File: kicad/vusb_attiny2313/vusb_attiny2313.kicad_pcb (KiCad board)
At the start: 2 copper layers, 64.9 x 49.4 mm, 24 parts, among them J1 USB_B_Micro, J2 PORT, J3 PORT B, J4 PORT A, Q1 BSS138, SW1 SW_SPST, U1 LM1117-1.8, U2 ATTINY2313-20PU, U3 MCP23S17, Y1 12Mhz

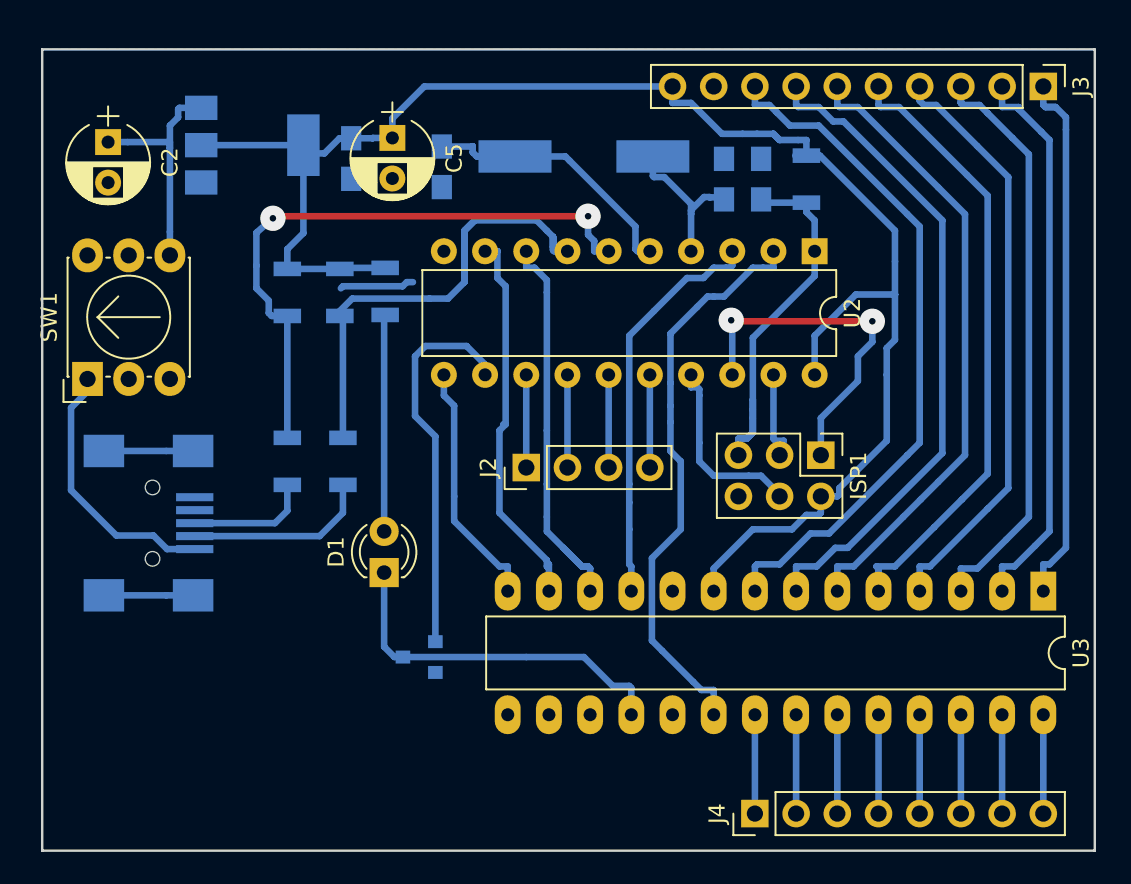
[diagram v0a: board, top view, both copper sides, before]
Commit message: first revision, kernel and avr part work. Kernel code have to be refine
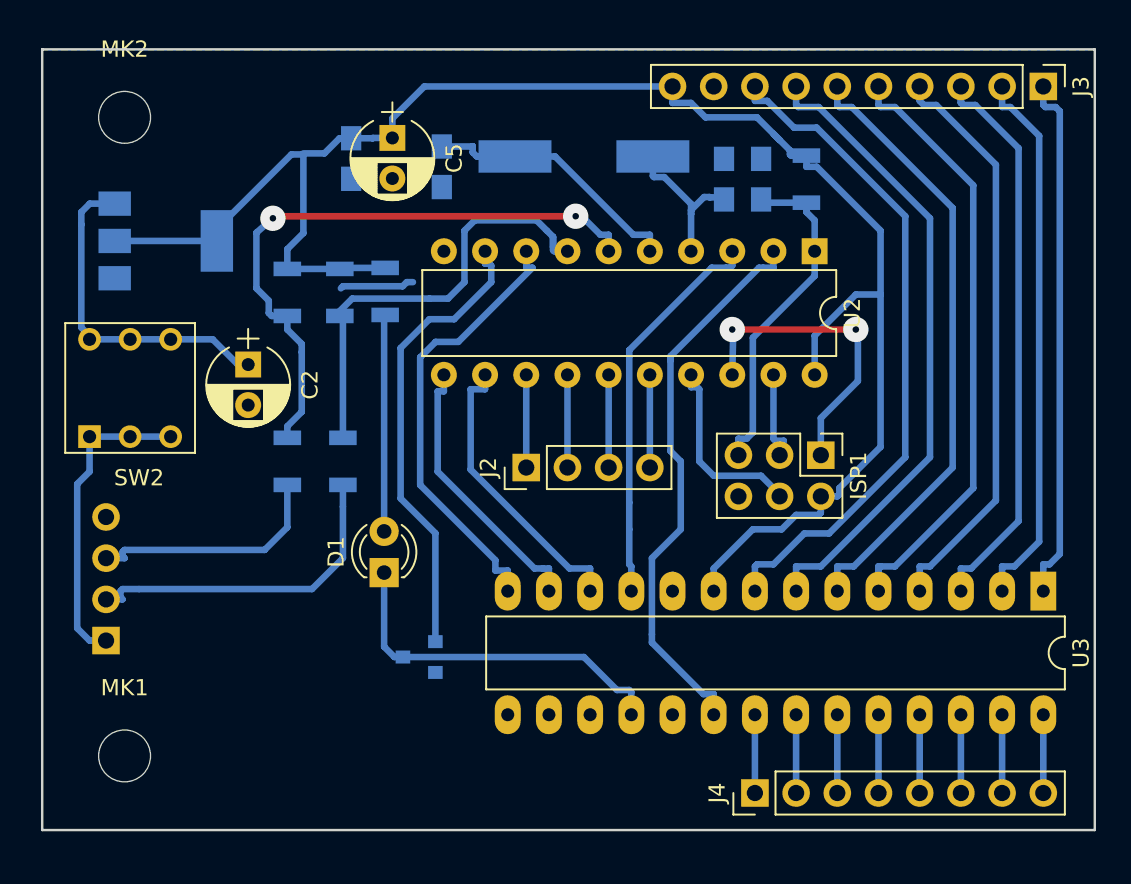
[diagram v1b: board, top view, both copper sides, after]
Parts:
- removed SW1: SW_SPST, Buttons_Switches_THT:Nidec_Copal_SH-7010C
- added MK1: Mounting_Hole, Mounting_Holes:MountingHole_3.2mm_M3, F.Cu at (35.6, 63.5)
- added MK2: Mounting_Hole, Mounting_Holes:MountingHole_3.2mm_M3, F.Cu at (35.6, 24.1)
- added SW2: SW_DIP_x03, Buttons_Switches_THT:SW_PUSH_x2, F.Cu at (33.4, 43.8)
- J1: footprint Connectors:USB_Mini-B -> Pin_Headers:Pin_Header_Straight_1x04_Pitch2.54mm
- moved C2 16.2 mm to (43.2, 39.4)
- moved U1 7.96 mm to (38.1, 31.8)
- moved J1 7.71 mm to (34.4, 56.4)
- moved J4 1.27 mm to (74.4, 65.8)
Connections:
- net Net-(U2-Pad3) renamed /DATA_CS
- Q1 pad 1: Net-(Q1-Pad1) -> /LED
- U2 pad 11: Net-(U2-Pad11) -> /DATA_IN
- U2 pad 12: Net-(Q1-Pad1) -> /DATA_SCK
- U2 pad 8: Net-(U2-Pad8) -> /DATA_OUT
- U2 pad 9: Net-(U2-Pad9) -> /LED
- U3 pad 12: Net-(U2-Pad8) -> /DATA_SCK
- U3 pad 13: Net-(U2-Pad9) -> /DATA_IN
- U3 pad 14: Net-(U2-Pad11) -> /DATA_OUT
- U3 pad 15: Net-(U3-Pad15) -> (no net)
- U3 pad 16: Net-(U3-Pad16) -> (no net)
- U3 pad 17: Net-(U3-Pad17) -> (no net)
- U3 pad 19: /INTB -> (no net)
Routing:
- net /LED: track 0.00 -> 28.5 mm
- net /DATA_OUT: track 0.00 -> 28.5 mm
- net Net-(U2-Pad8): track 27.1 -> 0.00 mm
- net Net-(U2-Pad9): track 25.4 -> 0.00 mm
- net Net-(Q1-Pad1): track 23.8 -> 0.00 mm
- net /DATA_SCK: track 0.00 -> 18.0 mm
- net /DATA_IN: track 0.00 -> 17.2 mm
- net Net-(U2-Pad11): track 15.4 -> 0.00 mm
- net Net-(J1-Pad6): track 11.0 -> 0.00 mm
- net Net-(J1-Pad2): track 11.5 -> 20.7 mm
- net Net-(J1-Pad3): track 7.62 -> 15.0 mm
- net Net-(C2-Pad1): track 14.9 -> 20.7 mm
- net /D-: track 34.1 -> 29.2 mm
- net /RST: track 24.5 -> 20.9 mm
- net VCC: track 106.8 -> 110.0 mm
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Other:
- board size 64.9 x 49.4 mm -> 64.9 x 48.1 mm

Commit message: Add label to the board
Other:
- board text added: "- +"
- board text added: "1 2 3 4"
- board text added: "AT_PORT_B"
- board text added: "ISP"
- board text added: "PA0 PA1 PA2 PA3 PA4 PA5 PA6 PA7"
- board text added: "PB0 PB1 PB2 PB3 PB4 PB5 PB6 PB7 GND VCC"
- board text added: "PD2 D+ PD3 D- PD0 INTA PD1 DATA_CS PD4 DATA_OUT PD5 LED PD6 DATA_IN"
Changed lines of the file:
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@@
-(kicad_pcb (version 20171130) (host pcbnew no-vcs-found-70f516b~61~ubuntu16.04.1)
+(kicad_pcb (version 20171130) (host pcbnew 5.0-dev-unknown-dd04bcb~61~ubuntu16.04.1)
   (general
     (thickness 1.6)
-    (drawings 4)
+    (drawings 11)
     (tracks 341)
     (zones 0)
@@
     )
   )
+  (gr_text "PD2 D+ \nPD3 D-\nPD0 INTA\nPD1 DATA_CS\nPD4 DATA_OUT\nPD5 LED\nPD6 DATA_IN" (at 40.64 63.5) (layer F.CrtYd)
+    (effects (font (size 1.5 1.5) (thickness 0.3)) (justify left))
+  )
+  (gr_text ISP (at 81.788 46.228 90) (layer F.CrtYd)
+    (effects (font (size 1.5 1.5) (thickness 0.3)))
+  )
+  (gr_text "-   +" (at 76.2 50.292) (layer F.CrtYd)
+    (effects (font (size 1.5 1.5) (thickness 0.3)))
+  )
+  (gr_text AT_PORT_B (at 64.008 42.672) (layer F.CrtYd)
+    (effects (font (size 1.5 1.5) (thickness 0.3)))
+  )
+  (gr_text "1\n2\n3\n4\n" (at 64.516 48.768 90) (layer F.CrtYd)
+    (effects (font (size 1.5 1.5) (thickness 0.3)))
+  )
+  (gr_text "PA0\nPA1\nPA2\nPA3\nPA4\nPA5\nPA6\nPA7\n" (at 83.312 70.104 90) (layer F.CrtYd)
+    (effects (font (size 1.5 1.5) (thickness 0.3)))
+  )
+  (gr_text "PB0\nPB1\nPB2\nPB3\nPB4\nPB5\nPB6\nPB7\nGND\nVCC" (at 80.772 17.78 270) (layer F.CrtYd)
+    (effects (font (size 1.5 1.5) (thickness 0.3)))
+  )
   (gr_line (start 95.377 68.072) (end 95.377 19.939) (angle 90) (layer Edge.Cuts) (width 0.15))

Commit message: schematic done
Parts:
- removed J2: PORT, Socket_Strips:Socket_Strip_Straight_1x04_Pitch2.54mm
- removed J3: PORT B, Socket_Strips:Socket_Strip_Straight_1x10_Pitch2.54mm
- removed J4: PORT A, Socket_Strips:Socket_Strip_Straight_1x08_Pitch2.54mm
- added D2: SD 103BW, Diode_SMD:D_SOD-123, F.Cu at (175.3, 48.3)
- added D3: 1N4148, Diode_SMD:D_MiniMELF_Handsoldering, B.Cu at (149.4, 96.5)
- added D4: 1N4148, Diode_SMD:D_MiniMELF_Handsoldering, B.Cu at (149.4, 99.4)
- added D5: SD 103BW, Diode_SMD:D_SOD-123, F.Cu at (182.2, 46.5)
- added D6: SS14, Diode_SMD:D_SMA_Handsoldering, F.Cu at (182.8, 68.2)
- added H1: MH, MountingHole:MountingHole_3.2mm_M3_DIN965_Pad, F.Cu at (188.9, 73.2)
- added H2: MH, MountingHole:MountingHole_3.2mm_M3_DIN965_Pad, F.Cu at (199.3, 72.7)
- added L1: 330, Choke_SMD:Choke_CD75, F.Cu at (200.5, 65.6)
- added Q2: BSS138, Package_TO_SOT_SMD:SOT-23, F.Cu at (175.3, 43.2)
- added R7: 50, Resistor_SMD:R_0805_2012Metric_Pad1.15x1.40mm_HandSolder, F.Cu at (193.8, 75.0)
- added R8: 1M, Resistor_SMD:R_0805_2012Metric_Pad1.15x1.40mm_HandSolder, F.Cu at (193.8, 73.0)
- added R9: 10k, Resistor_SMD:R_0805_2012Metric_Pad1.15x1.40mm_HandSolder, F.Cu at (193.8, 71.1)
- added U4: 74HC595, Package_DIP:DIP-16_W7.62mm_Socket_LongPads, F.Cu at (132.9, 58.6)
- added U5: 27C256, modules:DIP_Socket-28pin_in_32_W11.9_W12.7_W15.24_W17.78_W18.5_3M_232-1285-00-0602J, F.Cu at (93.0, 43.6)
- added U6: LT1073CS, Package_SO:SOIC-8_3.9x4.9mm_P1.27mm, F.Cu at (182.0, 72.7)
- C1, C3, C4: footprint Capacitors_SMD:C_0805_HandSoldering -> Capacitor_SMD:C_0805_2012Metric_Pad1.15x1.40mm_HandSolder
- C2: footprint Capacitors_THT:CP_Radial_D5.0mm_P2.50mm -> Capacitor_THT:CP_Radial_D5.0mm_P2.50mm
- C5: value 10µ -> 100u; footprint Capacitors_THT:CP_Radial_D5.0mm_P2.50mm -> Capacitor_Tantalum_SMD:CP_EIA-7343-15_Kemet-W_Pad2.25x2.55mm_HandSolder
- C6: value 100n -> 100u/63v; footprint Capacitors_SMD:C_0805_HandSoldering -> Capacitor_THT:CP_Radial_D8.0mm_P5.00mm; moved to F.Cu
- D1: footprint LEDs:LED_D3.0mm -> LED_THT:LED_D3.0mm
- ISP1: footprint Pin_Headers:Pin_Header_Straight_2x03_Pitch2.54mm -> Connector_PinHeader_2.54mm:PinHeader_2x03_P2.54mm_Vertical
- J1: value USB_B_Micro -> USB; footprint Pin_Headers:Pin_Header_Straight_1x04_Pitch2.54mm -> Connector_PinHeader_2.54mm:PinHeader_1x04_P2.54mm_Vertical; moved to F.Cu
- MK1, MK2: footprint Mounting_Holes:MountingHole_3.2mm_M3 -> MountingHole:MountingHole_3.2mm_M3
- Q1: footprint TO_SOT_Packages_SMD:SOT-23 -> Package_TO_SOT_SMD:SOT-23; moved to F.Cu
- R1, R2, R3, R4, R5: footprint Resistors_SMD:R_1206 -> Resistor_SMD:R_0805_2012Metric_Pad1.15x1.40mm_HandSolder
- R6: value 470 -> 960; footprint Resistors_SMD:R_1206 -> Resistor_SMD:R_0805_2012Metric_Pad1.15x1.40mm_HandSolder
- SW2: footprint Buttons_Switches_THT:SW_PUSH_x2 -> modules:DPDT_WIDE_54_54
- U1: value LM1117-1.8 -> 74HC595; footprint TO_SOT_Packages_SMD:SOT-223-3_TabPin2 -> Package_DIP:DIP-16_W7.62mm_Socket_LongPads; moved to F.Cu
- U2: footprint Housings_DIP:DIP-20_W7.62mm -> Package_DIP:DIP-20_W7.62mm_LongPads
- U3: value MCP23S17 -> 74HC595; footprint Housings_DIP:DIP-28_W7.62mm_LongPads -> Package_DIP:DIP-16_W7.62mm_Socket_LongPads
- Y1: footprint Crystals:Crystal_SMD_HC49-SD -> Crystal:Crystal_HC49-U_Vertical; moved to F.Cu
- moved MK2 173.2 mm to (207.6, 4.20)
- moved C6 145.3 mm to (189.5, 65.8), turned to 0 degrees
- moved C5 136.4 mm to (182.9, 64.0), turned to 0 degrees
- moved MK1 136.4 mm to (166.8, 26.2)
- moved Q1 129.0 mm to (181.8, 42.2), turned to 0 degrees
- moved SW2 126.0 mm to (150.7, 89.9)
- moved R6 122.0 mm to (156.5, 97.3)
- moved J1 119.5 mm to (152.7, 73.1)
- moved D1 113.1 mm to (152.1, 103.9), turned to 0 degrees
- moved C2 112.0 mm to (142.2, 91.7), turned to 90 degrees
- moved R4 111.5 mm to (146.3, 82.8), turned to 0 degrees
- moved R3 109.7 mm to (146.3, 85.3), turned to 0 degrees
- moved R1 108.5 mm to (148.8, 78.7), turned to 0 degrees
- moved R2 104.4 mm to (148.9, 75.9), turned to 0 degrees
- moved C4 84.4 mm to (115.6, 86.1), turned to 90 degrees
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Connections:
- net /MISO renamed /D6
- net /MOSI renamed /D5
- net /SCK renamed /D7
- C2 pad 1: Net-(C2-Pad1) -> +5V
- C5 pad 1: VCC -> +5V
- C6 pad 1: VCC -> +12V
- D1 pad 1: Net-(D1-Pad1) -> GND
- J1 pad 1: Net-(J1-Pad1) -> GND
- Q1 pad 1: /LED -> (no net)
- Q1 pad 2: GND -> /VPP
- Q1 pad 3: Net-(D1-Pad1) -> +12V
- R6 pad 1: VCC -> +5V
- SW2 pad 1: Net-(J1-Pad1) -> Net-(J1-Pad4)
- SW2 pad 2: Net-(J1-Pad1) -> Net-(J1-Pad4)
- SW2 pad 3: Net-(J1-Pad1) -> Net-(J1-Pad4)
- SW2 pad 4: Net-(C2-Pad1) -> +5V
- SW2 pad 5: Net-(C2-Pad1) -> +5V
- SW2 pad 6: Net-(C2-Pad1) -> +5V
- U1 pad 1: GND -> /~CE
- U1 pad 2: VCC -> /~OE
- U1 pad 3: Net-(C2-Pad1) -> (no net)
- U2 pad 11: /DATA_IN -> (no net)
- U2 pad 12: /DATA_SCK -> /D0
- U2 pad 13: Net-(J2-Pad1) -> /D1
- U2 pad 14: Net-(J2-Pad2) -> /D2
- U2 pad 15: Net-(J2-Pad3) -> /D3
- U2 pad 16: Net-(J2-Pad4) -> /D4
- U2 pad 2: /INTA -> /DATA_SCK
- U2 pad 3: /DATA_CS -> /DATA_IN
- U2 pad 8: /DATA_OUT -> /DATA_CS
- U2 pad 9: /LED -> /DATA_CLR
- U3 pad 10: GND -> /DATA_CLR
- U3 pad 11: /DATA_CS -> /DATA_SCK
- U3 pad 12: /DATA_SCK -> /DATA_CS
- U3 pad 13: /DATA_IN -> GND
- U3 pad 14: /DATA_OUT -> /DATA_IN
- U3 pad 15: (no net) -> Net-(U3-Pad15)
- U3 pad 16: (no net) -> VCC
- U3 pad 8: Net-(J3-Pad8) -> GND
- U3 pad 9: VCC -> /DATA_Q
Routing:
- net VCC: track 110.0 -> 0.00 mm
- net Net-(J3-Pad8): track 41.5 -> 0.00 mm
- net Net-(U3-Pad5): track 39.9 -> 0.00 mm
- net Net-(U3-Pad7): track 39.6 -> 0.00 mm
- net /D+: track 38.8 -> 0.00 mm, vias 2 -> 0
- net Net-(U3-Pad6): track 38.0 -> 0.00 mm
- net Net-(U3-Pad4): track 35.8 -> 0.00 mm
- net Net-(U3-Pad3): track 35.3 -> 0.00 mm
- net /INTA: track 34.7 -> 0.00 mm
- net Net-(U3-Pad2): track 33.8 -> 0.00 mm
- net Net-(U3-Pad1): track 32.6 -> 0.00 mm
- net /D-: track 29.2 -> 0.00 mm
- net /LED: track 28.5 -> 0.00 mm
- net /DATA_OUT: track 28.5 -> 0.00 mm
- net /DATA_CS: track 24.3 -> 0.00 mm
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- removed copper zone on B.Cu, net GND
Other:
- board outline removed
- board text removed: "- +"
- board text removed: "1 2 3 4"
- board text removed: "AT_PORT_B"
- board text removed: "ISP"
- board text removed: "PA0 PA1 PA2 PA3 PA4 PA5 PA6 PA7"
- board text removed: "PB0 PB1 PB2 PB3 PB4 PB5 PB6 PB7 GND VCC"
- board text removed: "PD2 D+ PD3 D- PD0 INTA PD1 DATA_CS PD4 DATA_OUT PD5 LED PD6 DATA_IN"
